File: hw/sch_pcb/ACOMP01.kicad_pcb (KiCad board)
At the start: 2 copper layers, 40.1 x 40.1 mm, 20 parts, among them IC1 TLV3604DCKR, IC2 LMH7220MK_NOPB, J1 Umin ... Umax, J2 Conn_Coaxial, J3 Conn_Coaxial, J4 Conn_Coaxial, J5 Conn_Coaxial, J6 HEADER_2x04_PARALLEL, J7 HEADER_2x04_PARALLEL, M1 HOLE M3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

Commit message: pcb layout
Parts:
- C2: value 100nF -> 1uF
- C3, C4, IC1, IC2, R1, R2: moved to B.Cu
- moved J7 63.3 mm to (132.1, 91.4), turned to 180 degrees
- moved J6 62.5 mm to (132.1, 101.6), turned to 180 degrees
- moved R1 45.0 mm to (128.3, 101.6), turned to 90 degrees
- moved C3 42.5 mm to (121.7, 101.6)
- moved C4 40.6 mm to (119.6, 91.2), turned to 180 degrees
- moved IC2 38.8 mm to (119.5, 87.9)
- moved R2 36.9 mm to (128.3, 91.4), turned to 90 degrees
- moved J2 36.6 mm to (121.9, 111.8)
- moved J5 36.6 mm to (121.9, 81.3)
- moved IC1 31.9 mm to (120.0, 104.6), turned to 90 degrees
- moved J1 19.1 mm to (123.2, 96.5), turned to 0 degrees
- moved J3 14.4 mm to (111.8, 101.6)
- moved J4 14.4 mm to (111.8, 91.4)
- moved D1 13.8 mm to (118.4, 96.5), turned to -90 degrees
- moved M1 10.2 mm to (132.1, 81.3)
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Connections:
- net /OUT+_LMH renamed /LMH_OUT+
- net /OUT+_TLV renamed /TLV_OUT+
- net /OUT-_LMH renamed /LMH_OUT-
- net /OUT-_TLV renamed /TLV_OUT-
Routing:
- net /LMH_OUT-: track 0.00 -> 15.2 mm
- net /LMH_OUT+: track 0.00 -> 15.2 mm
- net /IN-_TLV: track 0.00 -> 8.51 mm
- net /IN+_TLV: track 0.00 -> 8.09 mm
- net /IN-_LMH: track 0.00 -> 7.74 mm
- net /IN+_LMH: track 0.00 -> 7.74 mm
- net /TLV_OUT-: track 0.00 -> 5.20 mm
- net /TLV_OUT+: track 0.00 -> 5.20 mm
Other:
- board size 40.1 x 40.1 mm -> 30 x 40.1 mm

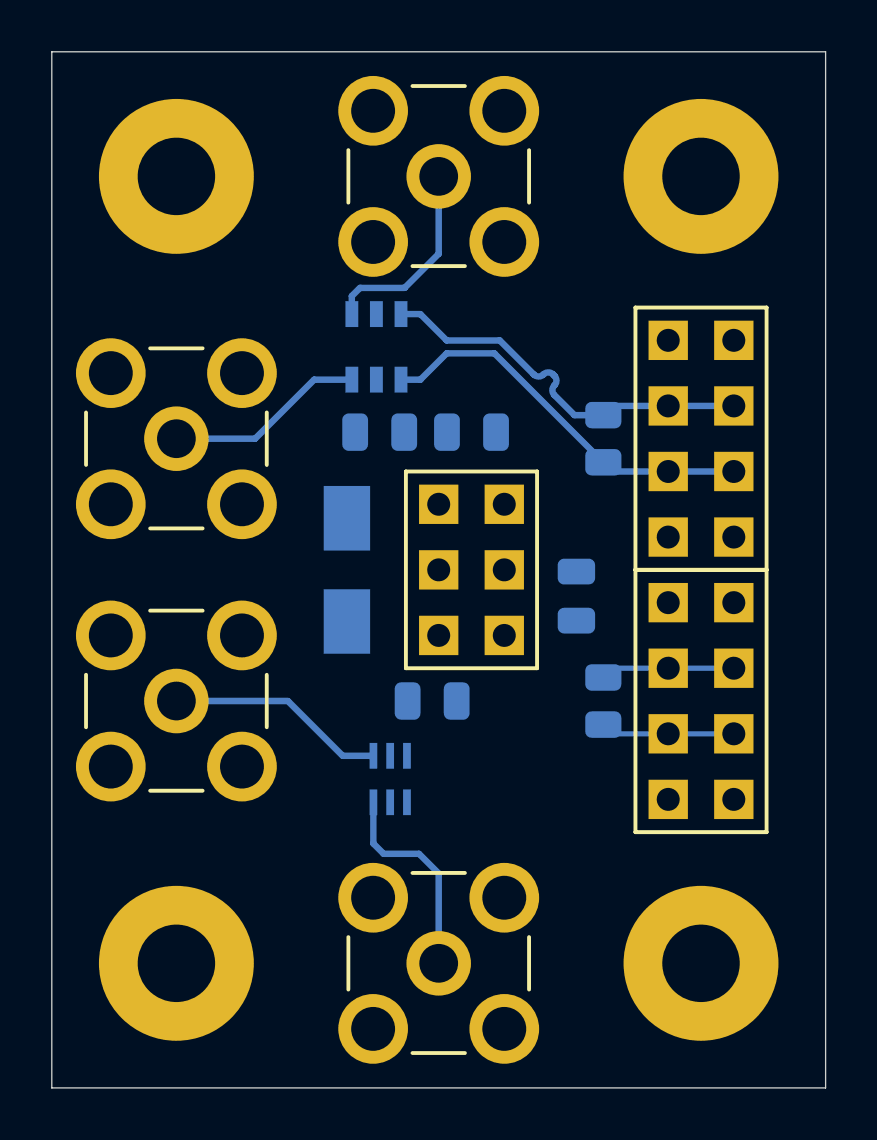
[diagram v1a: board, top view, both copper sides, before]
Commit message: pcb layout finished, ready for check
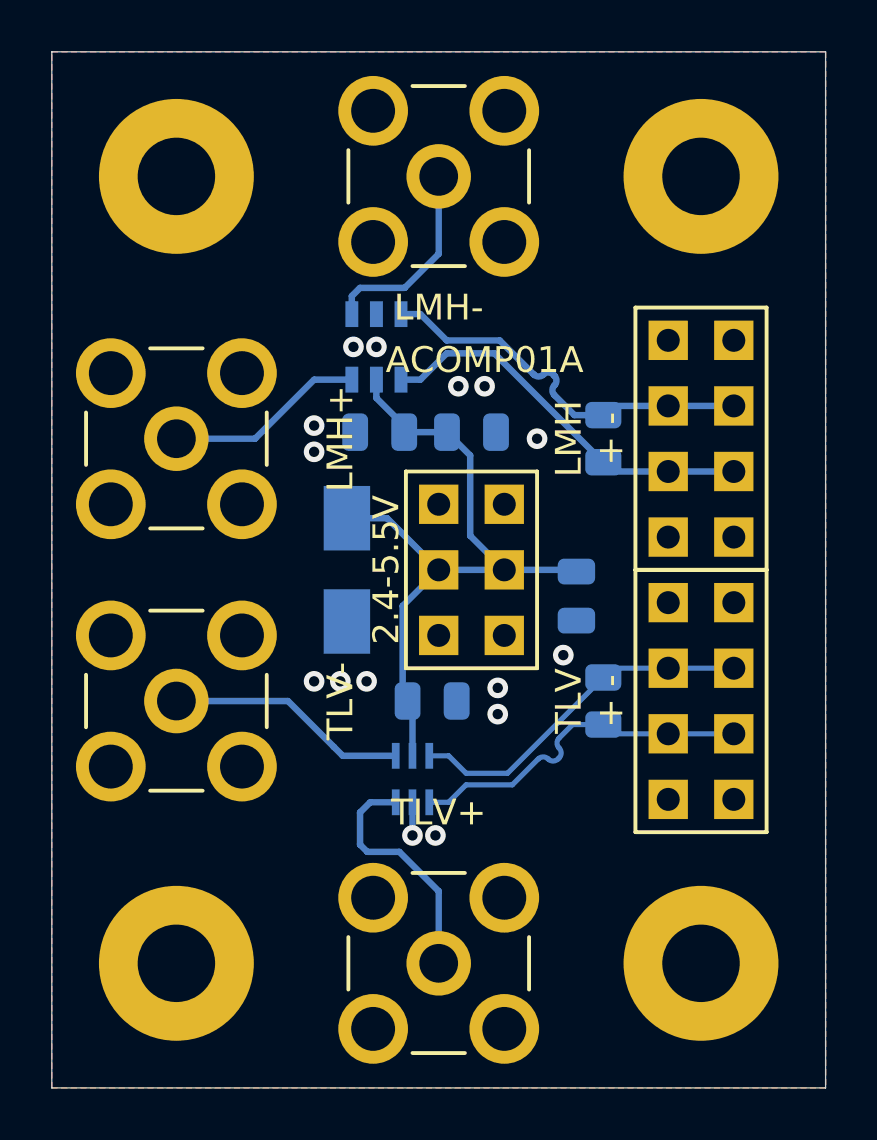
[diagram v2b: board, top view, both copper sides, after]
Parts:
- moved IC1 0.86 mm to (120.9, 104.6)
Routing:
- net +3V3: track 0.00 -> 29.2 mm
- net /TLV_OUT+: track 5.20 -> 13.8 mm
- net /TLV_OUT-: track 5.20 -> 13.8 mm
- net /IN+_TLV: track 8.09 -> 9.38 mm
- net GND: track 0.00 -> 1.28 mm, vias 0 -> 15
- net /IN-_TLV: track 8.51 -> 9.38 mm
- added copper zone on B.Cu, net GND
- added copper zone on F.Cu, net GND
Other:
- board text added: "2.4-5.5V"
- board text added: "ACOMP01A"
- board text added: "LMH + -"
- board text added: "LMH+"
- board text added: "LMH-"
- board text added: "TLV + -"
- board text added: "TLV+"
- board text added: "TLV-"

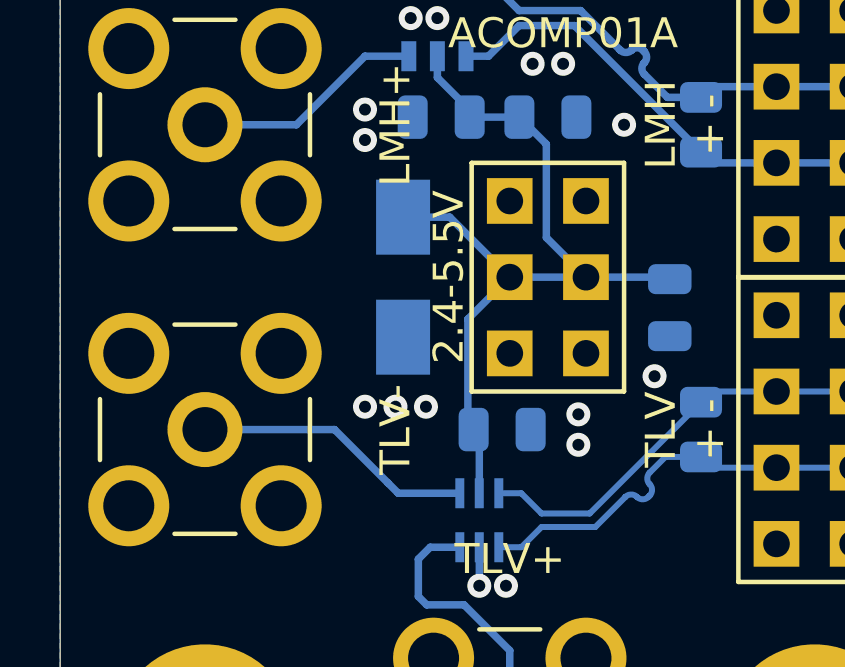
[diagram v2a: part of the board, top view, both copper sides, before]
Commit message: Cleanup of some DRC errors.
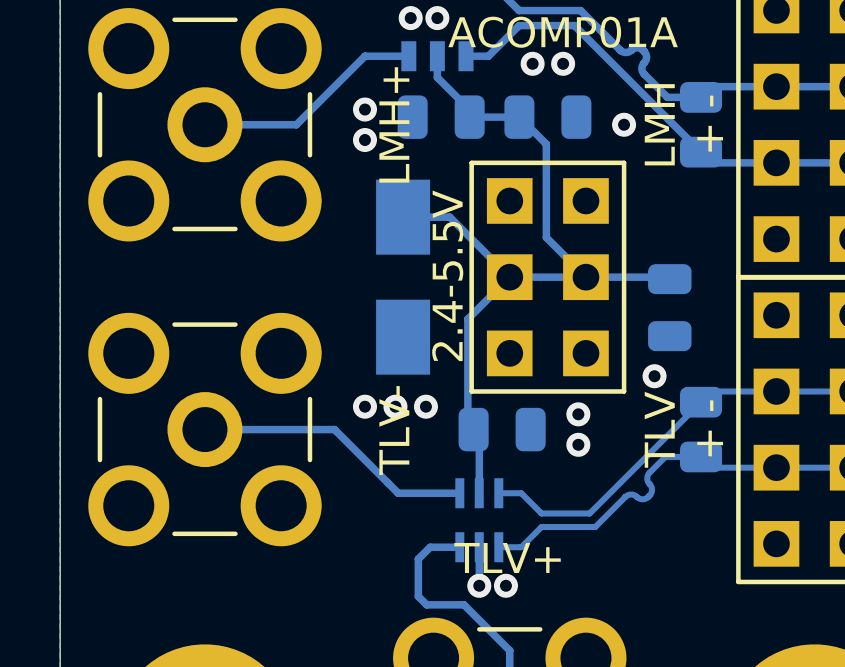
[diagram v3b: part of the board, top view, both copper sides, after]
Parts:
- J1: value Umin ... Umax -> 2,4 - 5,5V
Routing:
- net +3V3: track 29.2 -> 28.1 mm
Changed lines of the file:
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@@
       (effects (font (size 1.5 1.5) (thickness 0.15)))
     )
-    (fp_text value "Umin ... Umax" (at 0 5.08) (layer "F.SilkS") hide
+    (fp_text value "2,4 - 5,5V" (at 0 5.08) (layer "F.SilkS") hide
       (effects (font (size 1.5 1.5) (thickness 0.15)))
     )
@@
     (property "Sheetname" "")
     (attr smd)
-    (fp_text reference "C4" (at 2.794 0) (layer "B.SilkS")
+    (fp_text reference "C4" (at 2.8702 0.2286) (layer "B.SilkS")
       (effects (font (size 1 1) (thickness 0.15)) (justify mirror))
     )
@@
     (property "Sheetname" "")
     (attr smd)
-    (fp_text reference "C3" (at -2.794 0) (layer "B.SilkS")
+    (fp_text reference "C3" (at -2.7686 0.635) (layer "B.SilkS")
       (effects (font (size 1 1) (thickness 0.15)) (justify mirror))
     )
@@
     (property "UST_id" "C0805_100n")
     (attr smd)
-    (fp_text reference "C2" (at 2.794 0) (layer "B.SilkS")
+    (fp_text reference "C2" (at 2.7178 -0.8128) (layer "B.SilkS")
       (effects (font (size 1 1) (thickness 0.15)) (justify mirror))
     )
@@
     (pts (xy 111.76 81.28) (xy 111.76 111.76))
     (height 7.62)
-    (gr_text "30.4800 mm" (at 102.99 96.52 90) (layer "Dwgs.User")
+    (gr_text "1200,0000 mils" (at 102.99 96.52 90) (layer "Dwgs.User")
       (effects (font (size 1 1) (thickness 0.15)))
     )
@@
     (pts (xy 136.906 76.454) (xy 136.906 116.586))
     (height -2.794)
-    (gr_text "40.1320 mm" (at 138.55 96.52 90) (layer "Dwgs.User")
+    (gr_text "1580,0000 mils" (at 138.55 96.52 90) (layer "Dwgs.User")
       (effects (font (size 1 1) (thickness 0.15)))
     )
@@
     (pts (xy 136.906 76.454) (xy 106.934 76.454))
     (height 2.794)
-    (gr_text "29.9720 mm" (at 121.92 72.51) (layer "Dwgs.User")
+    (gr_text "1180,0000 mils" (at 121.92 72.51) (layer "Dwgs.User")
       (effects (font (size 1 1) (thickness 0.15)))
     )
@@
     (pts (xy 111.76 111.76) (xy 132.08 111.76))
     (height 7.62)
-    (gr_text "20.3200 mm" (at 121.92 118.23) (layer "Dwgs.User")
+    (gr_text "800,0000 mils" (at 121.92 118.23) (layer "Dwgs.User")
       (effects (font (size 1 1) (thickness 0.15)))
     )
@@
   (target plus (at 111.76 111.76) (size 5) (width 0.0127) (layer "Edge.Cuts"))
   (target plus (at 111.76 111.76) (size 5) (width 0.0127) (layer "Edge.Cuts"))
-  (segment (start 118.364 93.406) (end 118.364 94.52) (width 0.25) (layer "B.Cu") (net 1))
   (segment (start 120.523 101.407) (end 120.716 101.6) (width 0.25) (layer "B.Cu") (net 1))
   (segment (start 121.92 96.52) (end 124.46 96.52) (width 0.25) (layer "B.Cu") (net 1))
@@
   (segment (start 121.92 108.966) (end 121.92 111.76) (width 0.25) (layer "B.Cu") (net 3))
   (segment (start 118.2026 103.7226) (end 117.856 103.376) (width 0.25) (layer "B.Cu") (net 4))
-  (segment (start 117.856 103.378) (end 117.856 103.376) (width 0.25) (layer "B.Cu") (net 4))
   (segment (start 120.254 103.7226) (end 118.2026 103.7226) (width 0.25) (layer "B.Cu") (net 4))
   (segment (start 116.08 101.6) (end 111.76 101.6) (width 0.25) (layer "B.Cu") (net 4))

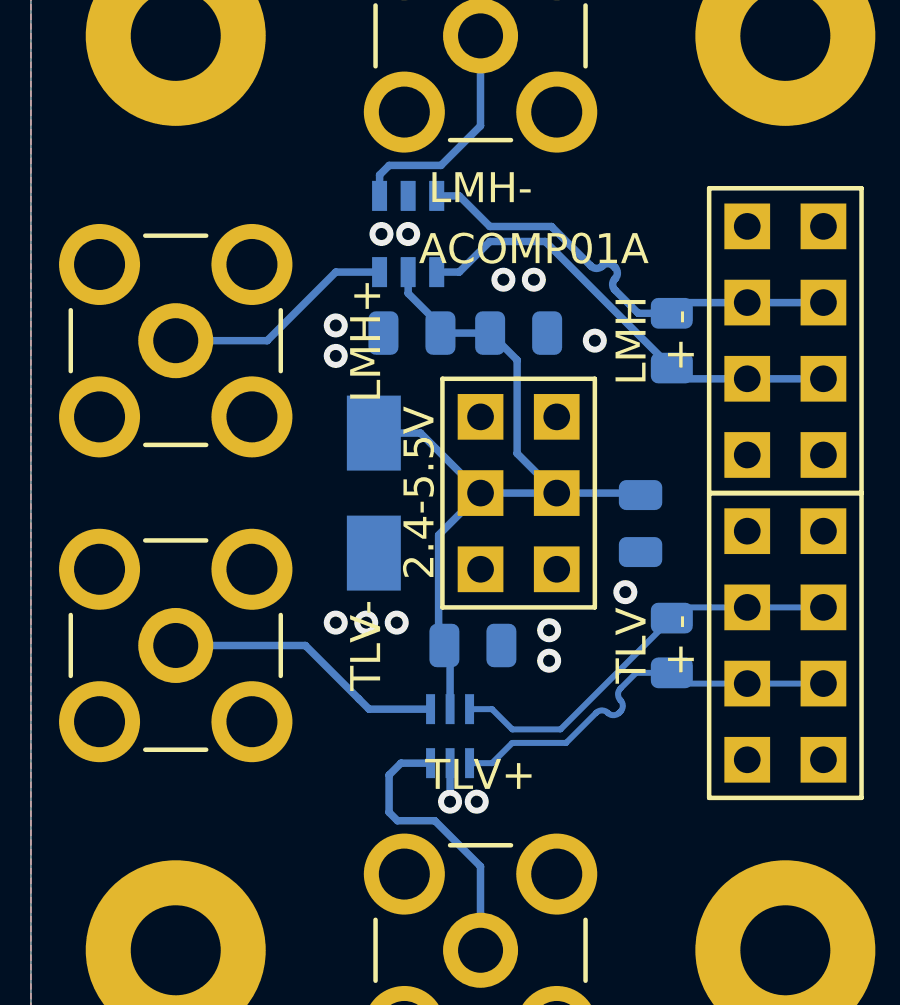
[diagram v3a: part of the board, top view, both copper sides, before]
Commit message: Update project to KiCADv9. Resolved #1
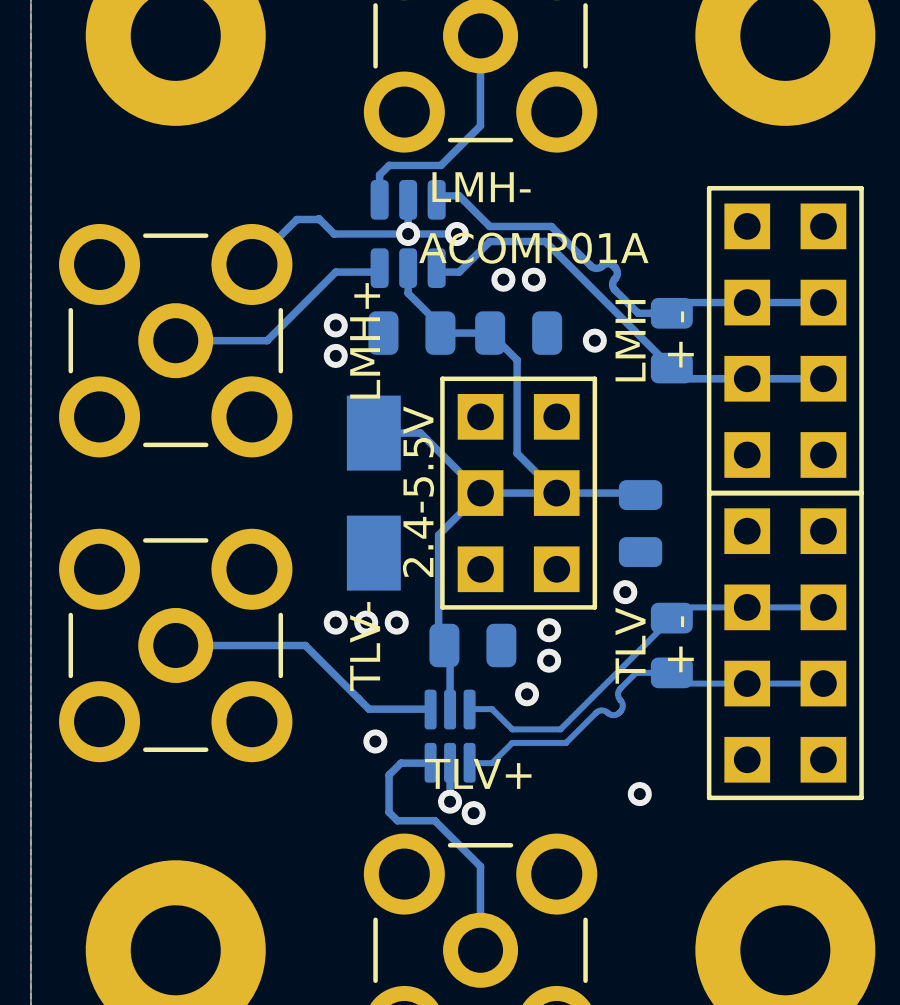
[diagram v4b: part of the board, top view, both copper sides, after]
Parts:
- IC1: footprint Mlab_IO:SC-70-6 -> Package_TO_SOT_SMD:SOT-363_SC-70-6
- IC2: footprint Mlab_IO:SOT-23-6 -> Package_TO_SOT_SMD:SOT-23-6
- turned IC2 to -90 degrees
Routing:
- net GND: track 1.28 -> 10.1 mm, vias 15 -> 18

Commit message: Improve documentation.
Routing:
- net GND: track 10.1 -> 13.9 mm
- net /IN+_TLV: track 9.38 -> 6.94 mm
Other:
- board text added: "2026"
